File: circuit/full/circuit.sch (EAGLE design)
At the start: 78 parts

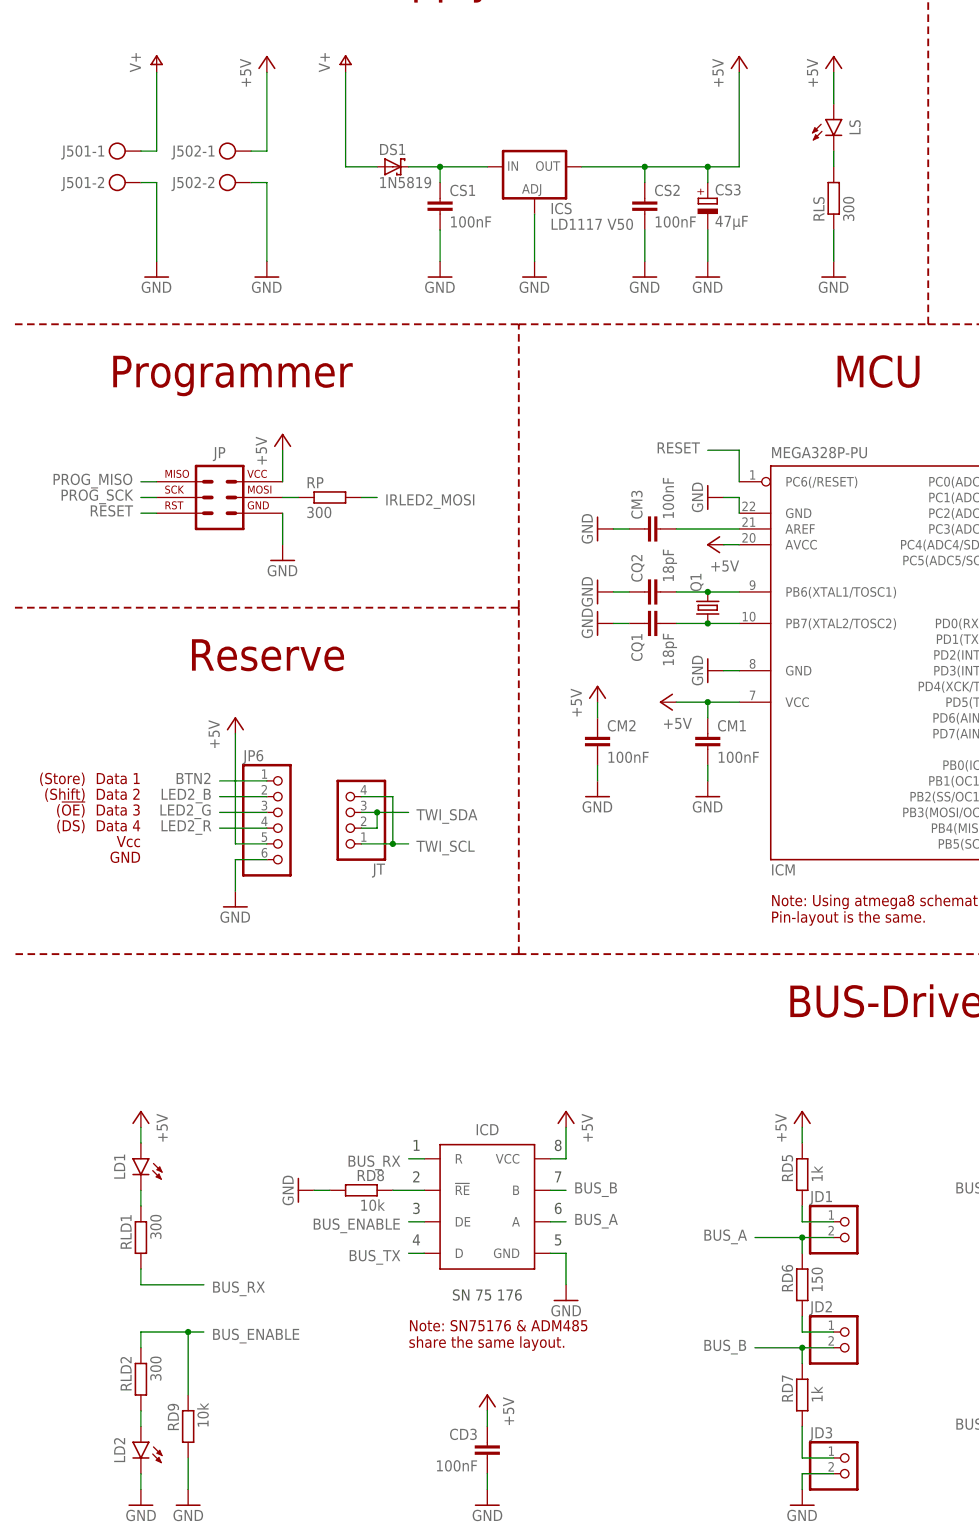
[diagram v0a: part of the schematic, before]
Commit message: updated circuit (added simplified version & minor bugfixes)
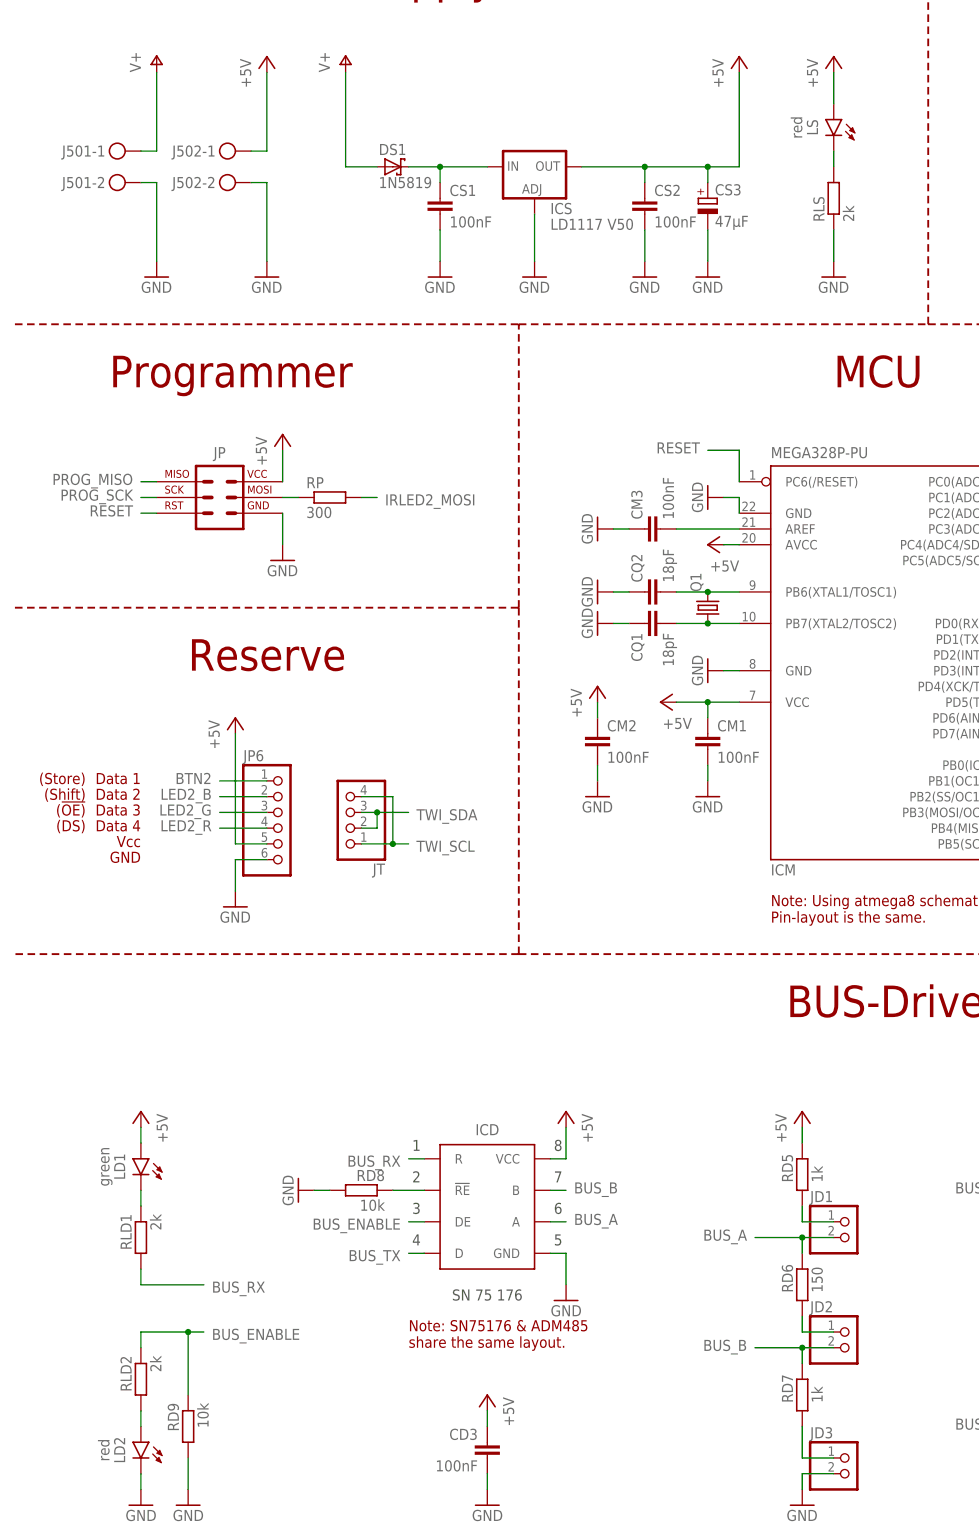
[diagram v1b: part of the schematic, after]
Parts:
- LD1: value (none) -> green
- LD2, LS: value (none) -> red
- RLD1, RLD2, RLS: value 300 -> 2k
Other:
- moved on the sheet: LS
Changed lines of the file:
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@@
 <part name="P+11" library="supply1" deviceset="+5V" device=""/>
 <part name="GND23" library="supply1" deviceset="GND" device=""/>
-<part name="LS" library="robo_ag" deviceset="LED" device="-3MM"/>
-<part name="RLS" library="rcl" deviceset="R-EU_" device="0207/10" value="300"/>
+<part name="LS" library="robo_ag" deviceset="LED" device="-3MM" value="red"/>
+<part name="RLS" library="rcl" deviceset="R-EU_" device="0207/10" value="2k"/>
 <part name="RL1R" library="rcl" deviceset="R-EU_" device="0207/10" value="40,4"/>
 <part name="RL1G" library="rcl" deviceset="R-EU_" device="0207/10" value="22"/>
@@
 <part name="GND35" library="supply1" deviceset="GND" device=""/>
 <part name="GND36" library="supply1" deviceset="GND" device=""/>
-<part name="LD2" library="robo_ag" deviceset="LED" device="-3MM"/>
-<part name="RLD2" library="rcl" deviceset="R-EU_" device="0207/10" value="300"/>
+<part name="LD2" library="robo_ag" deviceset="LED" device="-3MM" value="red"/>
+<part name="RLD2" library="rcl" deviceset="R-EU_" device="0207/10" value="2k"/>
 <part name="GND38" library="supply1" deviceset="GND" device=""/>
-<part name="LD1" library="robo_ag" deviceset="LED" device="-3MM"/>
-<part name="RLD1" library="rcl" deviceset="R-EU_" device="0207/10" value="300"/>
+<part name="LD1" library="robo_ag" deviceset="LED" device="-3MM" value="green"/>
+<part name="RLD1" library="rcl" deviceset="R-EU_" device="0207/10" value="2k"/>
 <part name="RD1" library="rcl" deviceset="R-EU_" device="0207/10" value="150"/>
 <part name="CD1" library="rcl" deviceset="C-EU" device="025-025X050" value="100pF"/>
@@
 <instance part="P+11" gate="1" x="132.08" y="243.84"/>
 <instance part="GND23" gate="1" x="132.08" y="208.28"/>
-<instance part="LS" gate="LED" x="132.08" y="233.68"/>
+<instance part="LS" gate="LED" x="132.08" y="233.68" rot="MR0"/>
 <instance part="RLS" gate="G$1" x="132.08" y="220.98" rot="R90"/>
 <instance part="RL1R" gate="G$1" x="337.82" y="170.18"/>

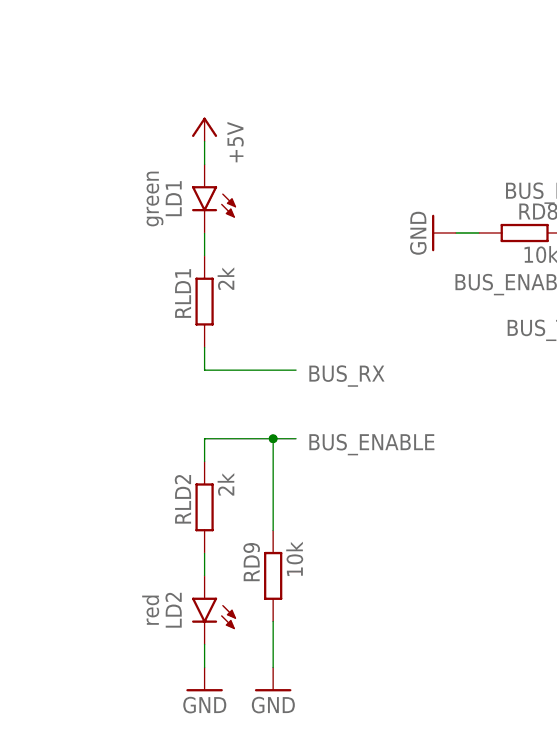
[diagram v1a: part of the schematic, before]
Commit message: switched color of LD1 and LD2 in full version
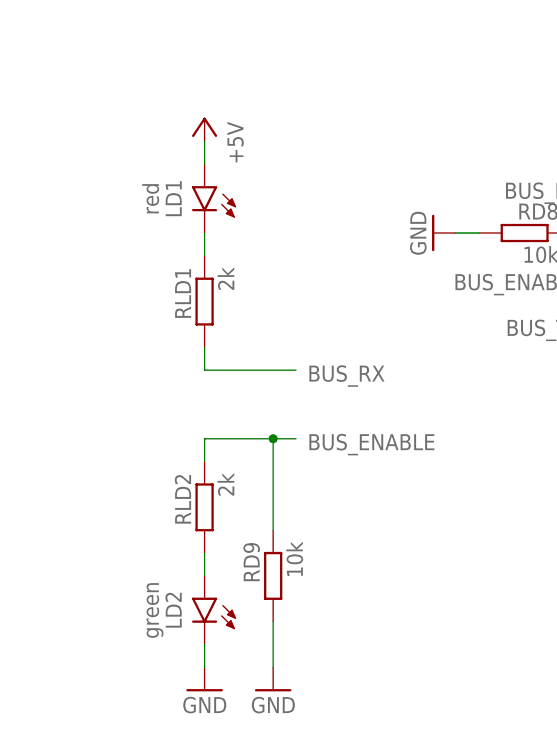
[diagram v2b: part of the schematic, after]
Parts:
- LD1: value green -> red
- LD2: value red -> green
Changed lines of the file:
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@@
 <part name="GND35" library="supply1" deviceset="GND" device=""/>
 <part name="GND36" library="supply1" deviceset="GND" device=""/>
-<part name="LD2" library="robo_ag" deviceset="LED" device="-3MM" value="red"/>
+<part name="LD2" library="robo_ag" deviceset="LED" device="-3MM" value="green"/>
 <part name="RLD2" library="rcl" deviceset="R-EU_" device="0207/10" value="2k"/>
 <part name="GND38" library="supply1" deviceset="GND" device=""/>
-<part name="LD1" library="robo_ag" deviceset="LED" device="-3MM" value="green"/>
+<part name="LD1" library="robo_ag" deviceset="LED" device="-3MM" value="red"/>
 <part name="RLD1" library="rcl" deviceset="R-EU_" device="0207/10" value="2k"/>
 <part name="RD1" library="rcl" deviceset="R-EU_" device="0207/10" value="150"/>
